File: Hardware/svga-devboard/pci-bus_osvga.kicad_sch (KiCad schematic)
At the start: 19 parts, among them J1 Bus_PCI_32bit_Universal_lrj

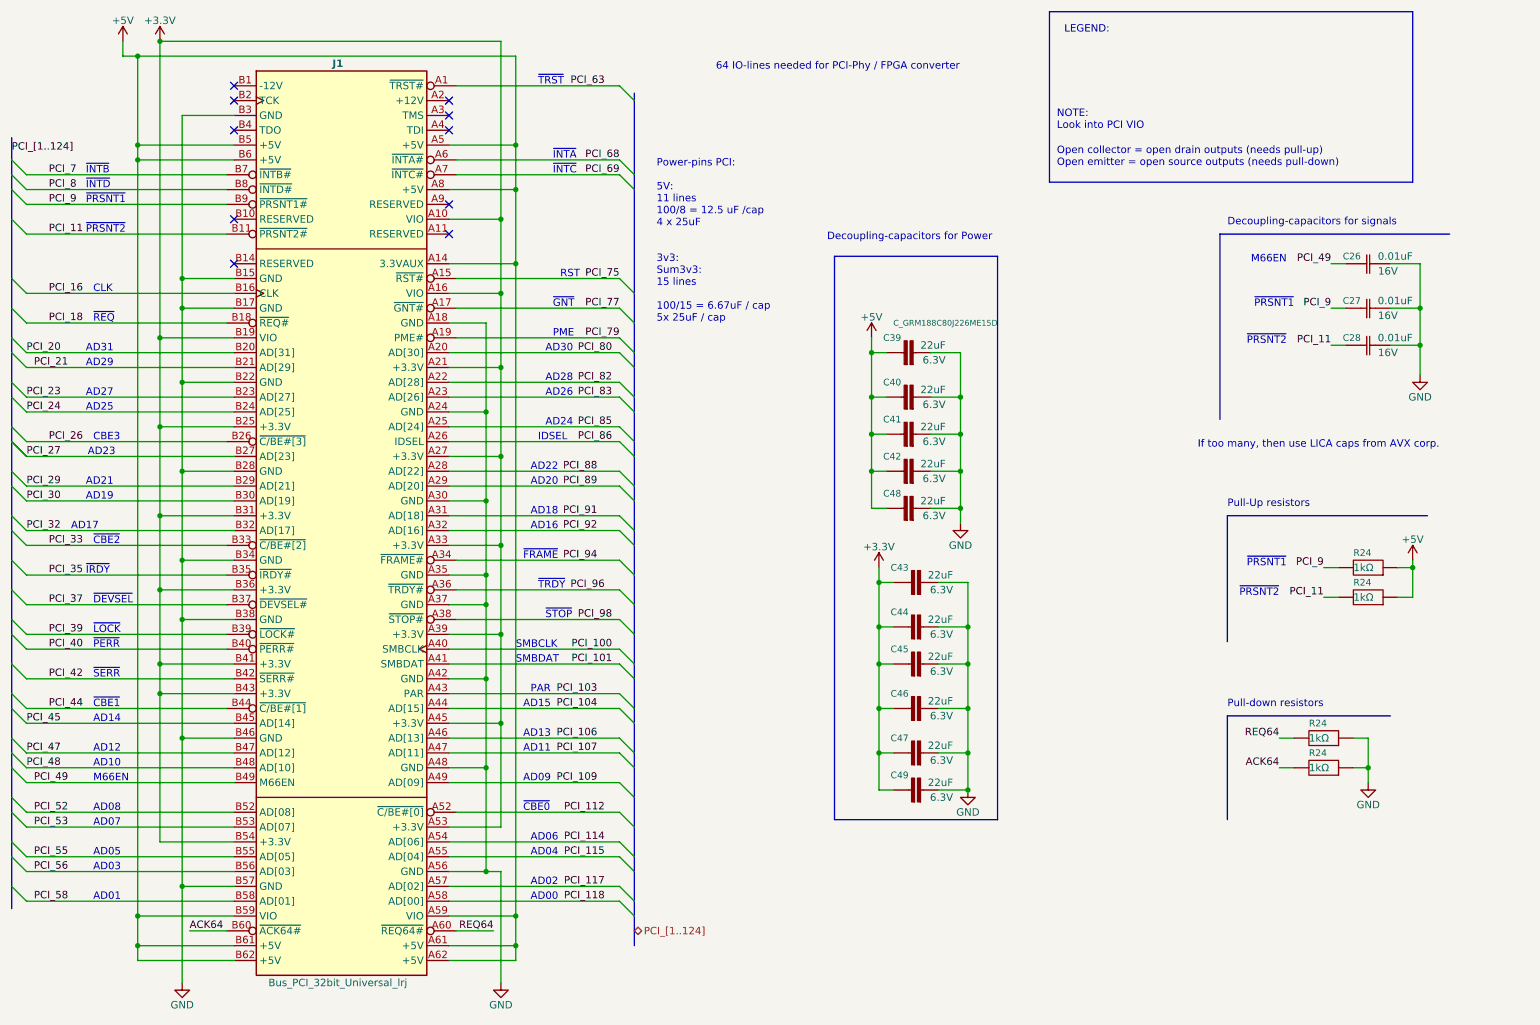
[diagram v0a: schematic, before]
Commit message: Disconnected the DVI-connectors from each other, so that they do go over the intended flat-cable to the daughter-board instead.
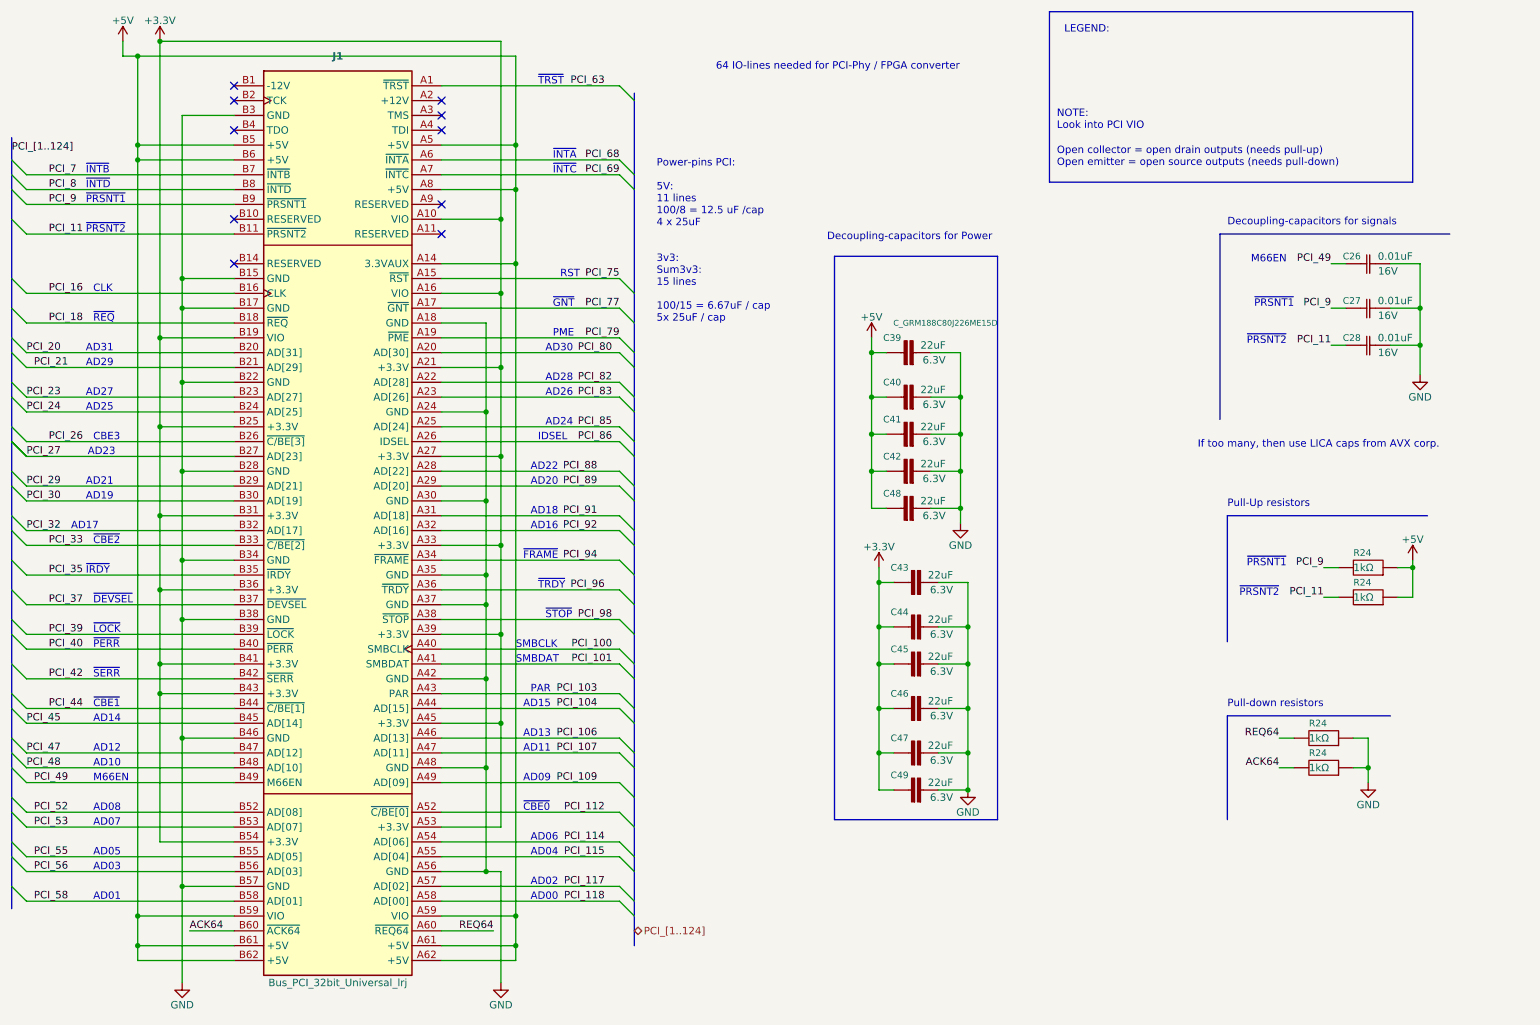
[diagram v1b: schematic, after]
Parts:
- J1: footprint Connector_PCBEdge:BUS_PCI_UNI_32-lrj2 -> LRJ:BUS_PCI_UNI_32; symbol LRJ-parts:Bus_PCI_32bit_Universal_lrj -> LRJ-parts:Bus_PCI_32bit_Universal-lrj; now left out of the parts list
